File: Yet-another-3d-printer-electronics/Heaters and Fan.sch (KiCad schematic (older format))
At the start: 54 parts, among them P15 HEATER_BED, P16 HEATER_EXT, P18 FAN, P22 FAN, P23 HEATER_EXT, P4 FAN, Q1 2N7000, Q2 IRLR8743PBF, Q3 IRLML0030TRPBF, Q4 IRLR8743PBF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

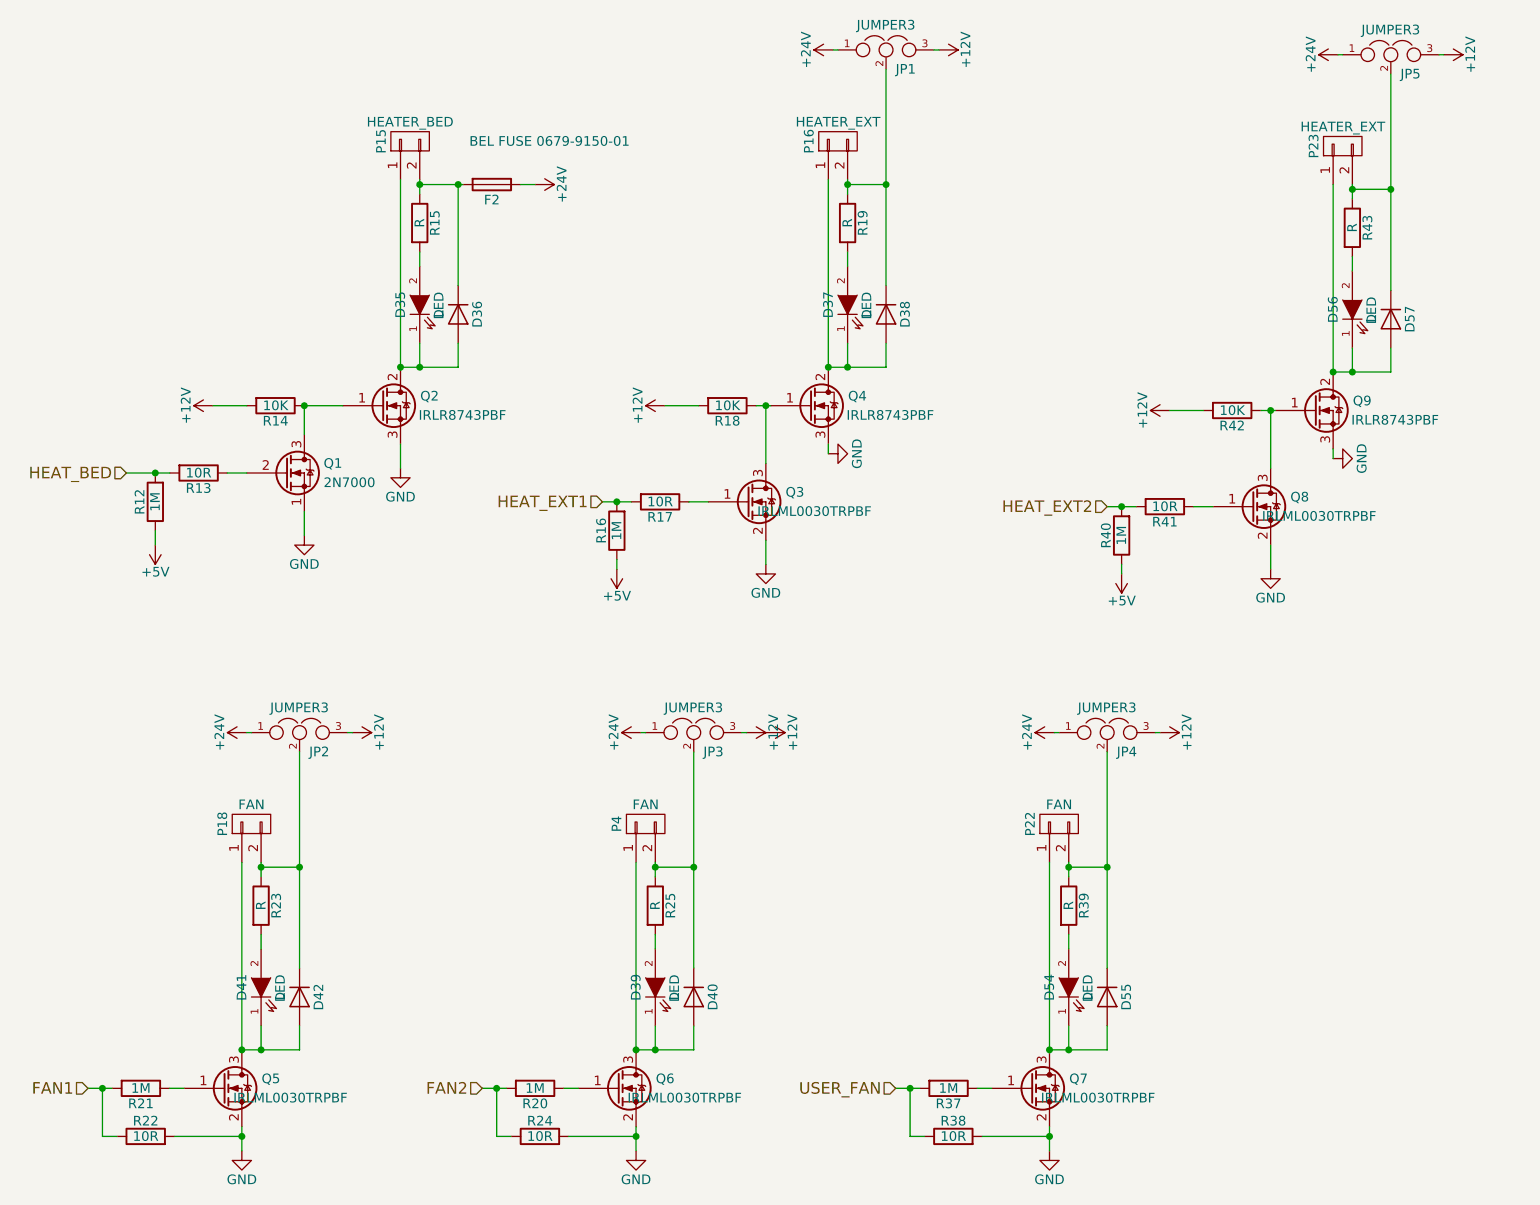
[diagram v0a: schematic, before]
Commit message: Add testpoints to Heaters and Fans
Signed-off-by: Mateusz Krawczuk <mat.krawczuk@gmail.com>
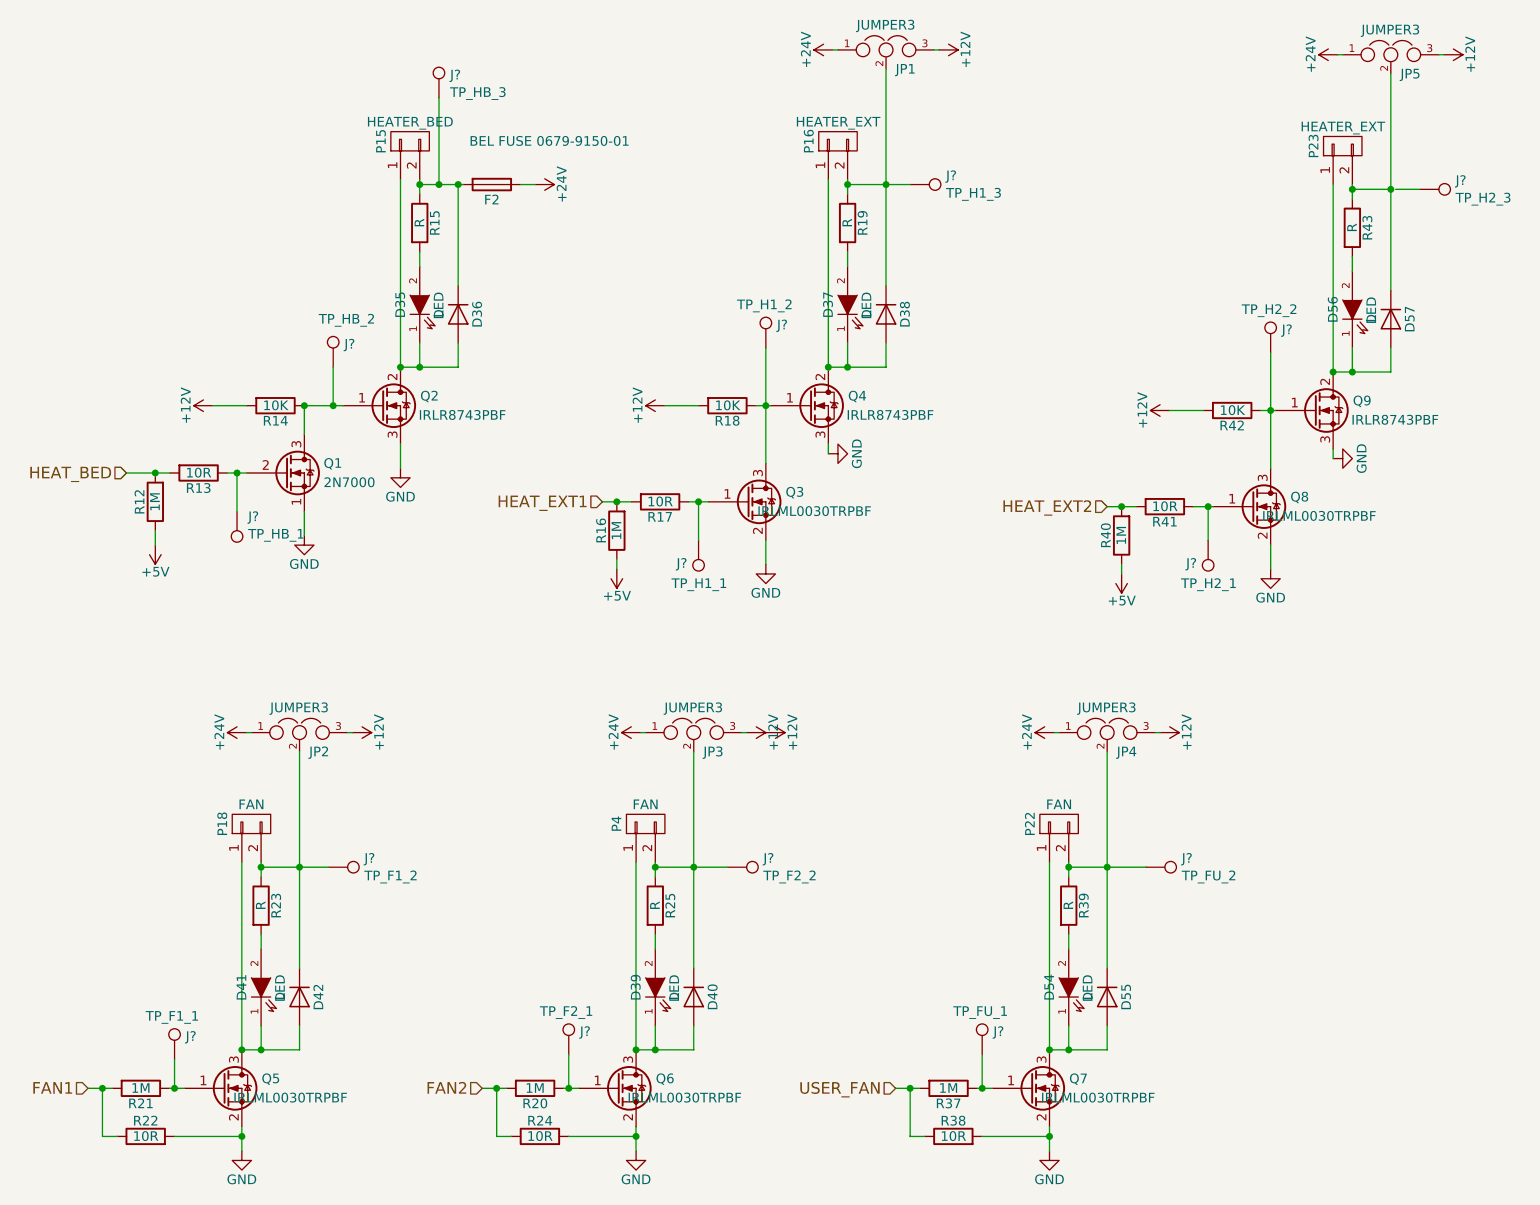
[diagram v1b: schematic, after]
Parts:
- added J?: TP_HB_3, symbol TEST_1P
- added J?: TP_H1_3, symbol TEST_1P
- added J?: TP_H2_3, symbol TEST_1P
- added J?: TP_F1_2, symbol TEST_1P
- added J?: TP_F2_2, symbol TEST_1P
- added J?: TP_FU_2, symbol TEST_1P
- added J?: TP_HB_2, symbol TEST_1P
- added J?: TP_HB_1, symbol TEST_1P
- added J?: TP_H1_2, symbol TEST_1P
- added J?: TP_H1_1, symbol TEST_1P
- added J?: TP_H2_1, symbol TEST_1P
- added J?: TP_H2_2, symbol TEST_1P
- added J?: TP_F1_1, symbol TEST_1P
- added J?: TP_F2_1, symbol TEST_1P
- added J?: TP_FU_1, symbol TEST_1P
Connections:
- net at D42.1 (K), JP2.2, P18.2 (P2)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: now also J?.1
- net at D38.1 (K), JP1.2, P16.2 (P2)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: now also J?.1
- net at Q1.3 (D), Q2.1 (G), R14.1: now also J?.1
- net at D36.1 (K), F2.2, P15.2 (P2)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: now also J?.1
- net at Q1.2 (G), R13.1: now also J?.1
- net at Q3.3 (D), Q4.1 (G), R18.1: now also J?.1
- net at Q5.1 (G), R21.1: now also J?.1
- net at Q3.1 (G), R17.1: now also J?.1
- net at D40.1 (K), JP3.2, P4.2 (P2)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: now also J?.1
- net at Q6.1 (G), R20.1: now also J?.1
- net at D55.1 (K), JP4.2, P22.2 (P2)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: now also J?.1
- net at Q7.1 (G), R37.1: now also J?.1
- net at Q8.3 (D), Q9.1 (G), R42.1: now also J?.1
- net at Q8.1 (G), R41.1: now also J?.1

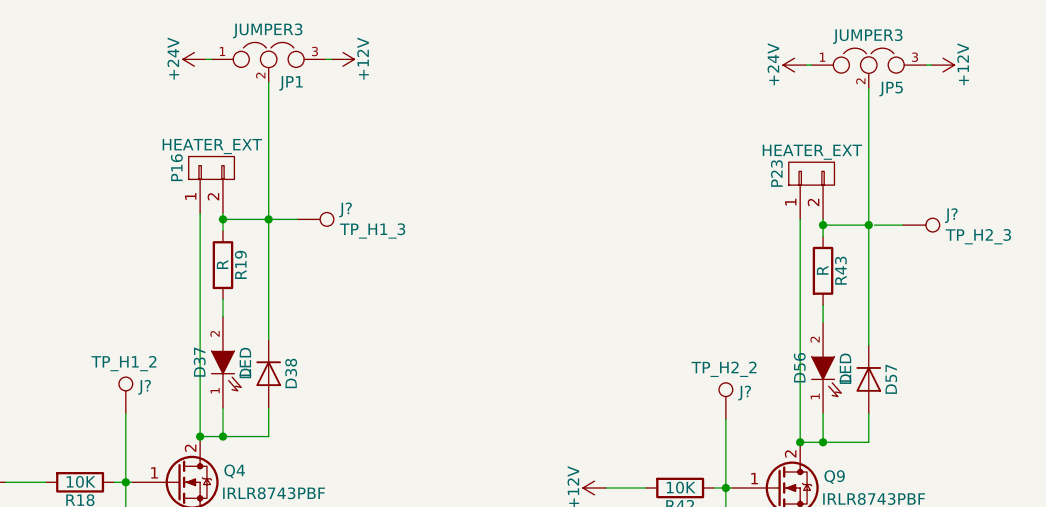
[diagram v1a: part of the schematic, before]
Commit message: Remove jumper for heaters
Jumper is removed due safety, Heaters at 12v can drain over 2A from pin
which is more than safety limit.

Signed-off-by: Mateusz Krawczuk <mat.krawczuk@gmail.com>
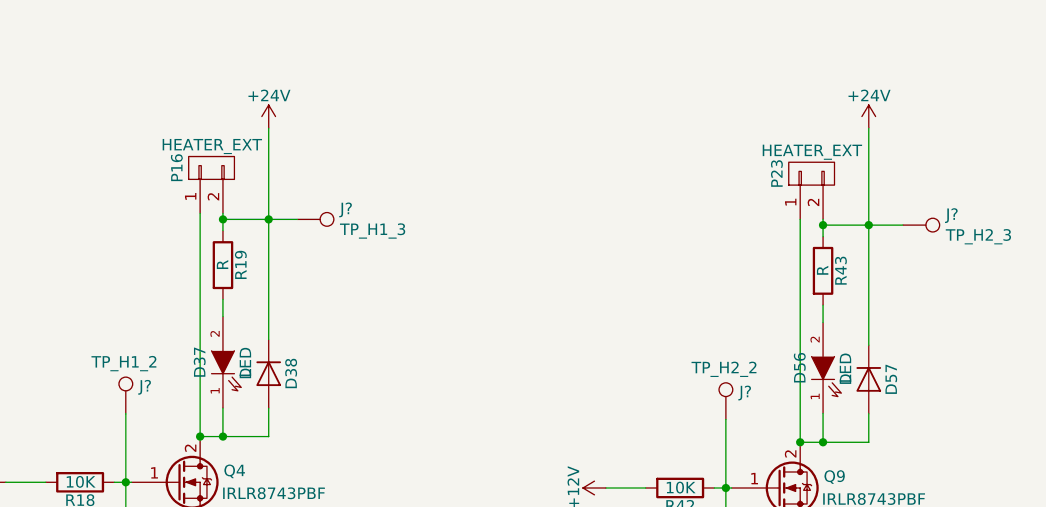
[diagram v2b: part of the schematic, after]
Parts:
- removed JP1, JP5: JUMPER3, symbol JUMPER3
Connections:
- net +24V: now also D38.1 (K), D57.1 (K), J?.1, J?.1, P16.2 (P2), P23.2 (P2), R19.1, R43.1
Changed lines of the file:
@@
 L +24V #PWR0115
 U 1 1 58B0BF44
-P 4750 1150
-F 0 "#PWR0115" H 4750 1000 50  0001 C CNN
-F 1 "+24V" H 4750 1290 50  0000 C CNN
-F 2 "" H 4750 1150 50  0000 C CNN
-F 3 "" H 4750 1150 50  0000 C CNN
-	1    4750 1150
-	0    -1   -1   0
-$EndComp
-$Comp
-L +12V #PWR0116
-U 1 1 58B0BF53
-P 5300 1150
-F 0 "#PWR0116" H 5300 1000 50  0001 C CNN
-F 1 "+12V" H 5300 1290 50  0000 C CNN
-F 2 "" H 5300 1150 50  0000 C CNN
-F 3 "" H 5300 1150 50  0000 C CNN
-	1    5300 1150
-	0    1    1    0
+P 5025 1450
+F 0 "#PWR0115" H 5025 1300 50  0001 C CNN
+F 1 "+24V" H 5025 1590 50  0000 C CNN
+F 2 "" H 5025 1450 50  0000 C CNN
+F 3 "" H 5025 1450 50  0000 C CNN
+	1    5025 1450
+	1    0    0    -1
 $EndComp
 $Comp
@@
 L +24V #PWR0130
 U 1 1 5902A5F3
-P 7375 1175
-F 0 "#PWR0130" H 7375 1025 50  0001 C CNN
-F 1 "+24V" H 7375 1315 50  0000 C CNN
-F 2 "" H 7375 1175 50  0000 C CNN
-F 3 "" H 7375 1175 50  0000 C CNN
-	1    7375 1175
-	0    -1   -1   0
-$EndComp
-$Comp
-L JUMPER3 JP5
-U 1 1 5902A5F9
-P 7650 1175
-F 0 "JP5" H 7700 1075 50  0000 L CNN
-F 1 "JUMPER3" H 7650 1275 50  0000 C BNN
-F 2 "" H 7650 1175 50  0001 C CNN
-F 3 "" H 7650 1175 50  0000 C CNN
-	1    7650 1175
-	1    0    0    -1
-$EndComp
-$Comp
-L +12V #PWR0131
-U 1 1 5902A5FF
-P 7925 1175
-F 0 "#PWR0131" H 7925 1025 50  0001 C CNN
-F 1 "+12V" H 7925 1315 50  0000 C CNN
-F 2 "" H 7925 1175 50  0000 C CNN
-F 3 "" H 7925 1175 50  0000 C CNN
-	1    7925 1175
-	0    1    1    0
+P 7650 1450
+F 0 "#PWR0130" H 7650 1300 50  0001 C CNN
+F 1 "+24V" H 7650 1590 50  0000 C CNN
+F 2 "" H 7650 1450 50  0000 C CNN
+F 3 "" H 7650 1450 50  0000 C CNN
+	1    7650 1450
+	1    0    0    -1
 $EndComp
 $Comp
@@
 	4825 2200 4825 2275
 Wire Wire Line
-	5025 1250 5025 2375
-Wire Wire Line
 	5025 2800 5025 2675
 Connection ~ 1225 3350
@@
 Wire Wire Line
 	2250 4700 2225 4700
-Wire Wire Line
-	4775 1150 4750 1150
-Wire Wire Line
-	5300 1150 5275 1150
 Connection ~ 5025 1850
 Wire Wire Line
@@
 	7450 2225 7450 2300
 Wire Wire Line
-	7650 1275 7650 2400
-Wire Wire Line
 	7650 2825 7650 2700
-Wire Wire Line
-	7400 1175 7375 1175
-Wire Wire Line
-	7925 1175 7900 1175
 Connection ~ 7650 1875
 Wire Wire Line
-	7650 1875 7450 1875
+	7450 1875 7800 1875
 Wire Wire Line
 	3200 1850 3125 1850
@@
 	0    1    1    0
 $EndComp
-Wire Wire Line
-	7800 1875 7675 1875
 $Comp
 L TEST_1P J?
@@
 	5525 6375 5525 6550
 Connection ~ 5525 6550
-$Comp
-L JUMPER3 JP1
-U 1 1 58B0BF4B
-P 5025 1150
-F 0 "JP1" H 5075 1050 50  0000 L CNN
-F 1 "JUMPER3" H 5025 1250 50  0000 C BNN
-F 2 "" H 5025 1150 50  0001 C CNN
-F 3 "" H 5025 1150 50  0000 C CNN
-	1    5025 1150
-	1    0    0    -1
-$EndComp
+Wire Wire Line
+	5025 1450 5025 2375
+Wire Wire Line
+	7650 1450 7650 2400
 $EndSCHEMATC
